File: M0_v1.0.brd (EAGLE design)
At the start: 68.6 x 53.3 mm, 61 parts, among them CN1 POWER_JACK, CN2 47346-0001, CN3 DIGITAL10, CN4 DIGITAL8, CN5 ICSP, CN6 POWER8, CN7 ANALOG6, CN8 SWD, CN9 UART, IC1 AMS1117-5.0, IC2 AMS1117-3.3, IC3 74LVC1G125DCK, Q2 32.768KHz, T1 AO3401A, T2 2N7002, U1 ATSAMD21G-AU, U2 ATSAMD21G-MU

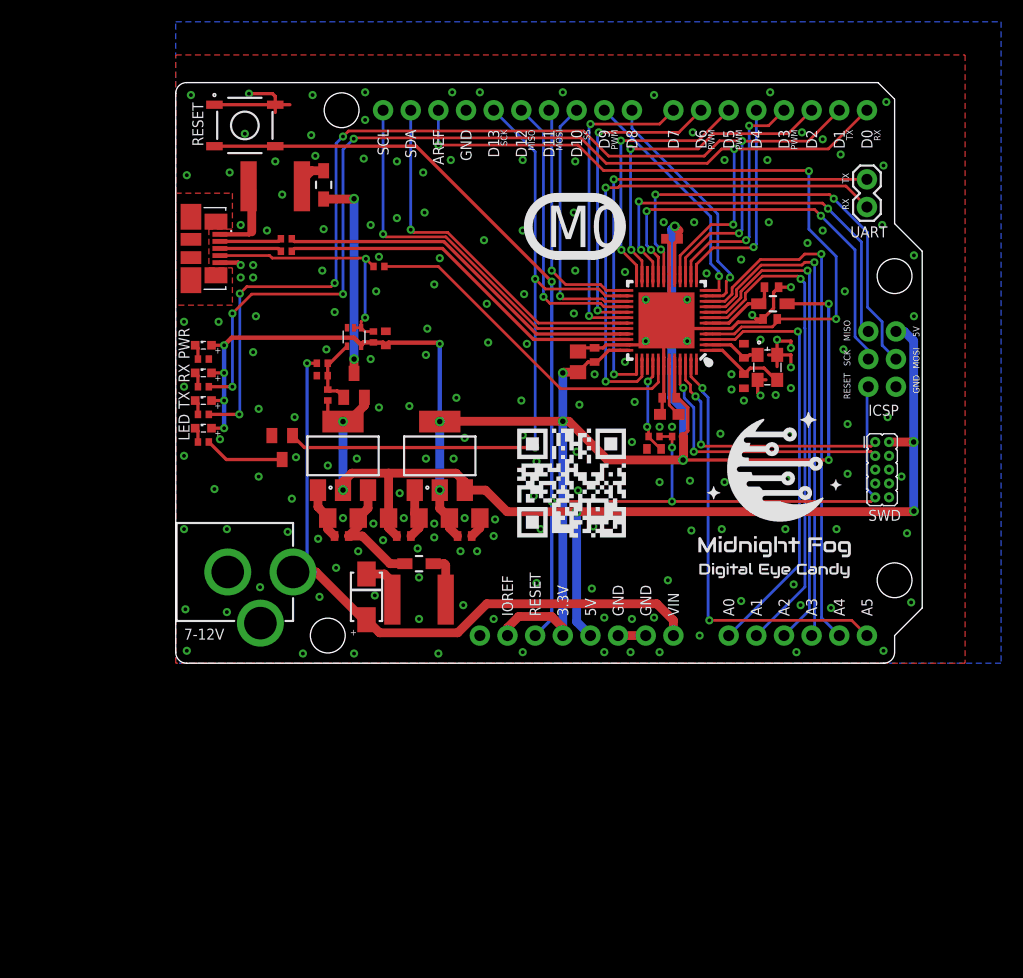
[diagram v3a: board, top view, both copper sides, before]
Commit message: Change the quote. Add some vias. move some traces around.
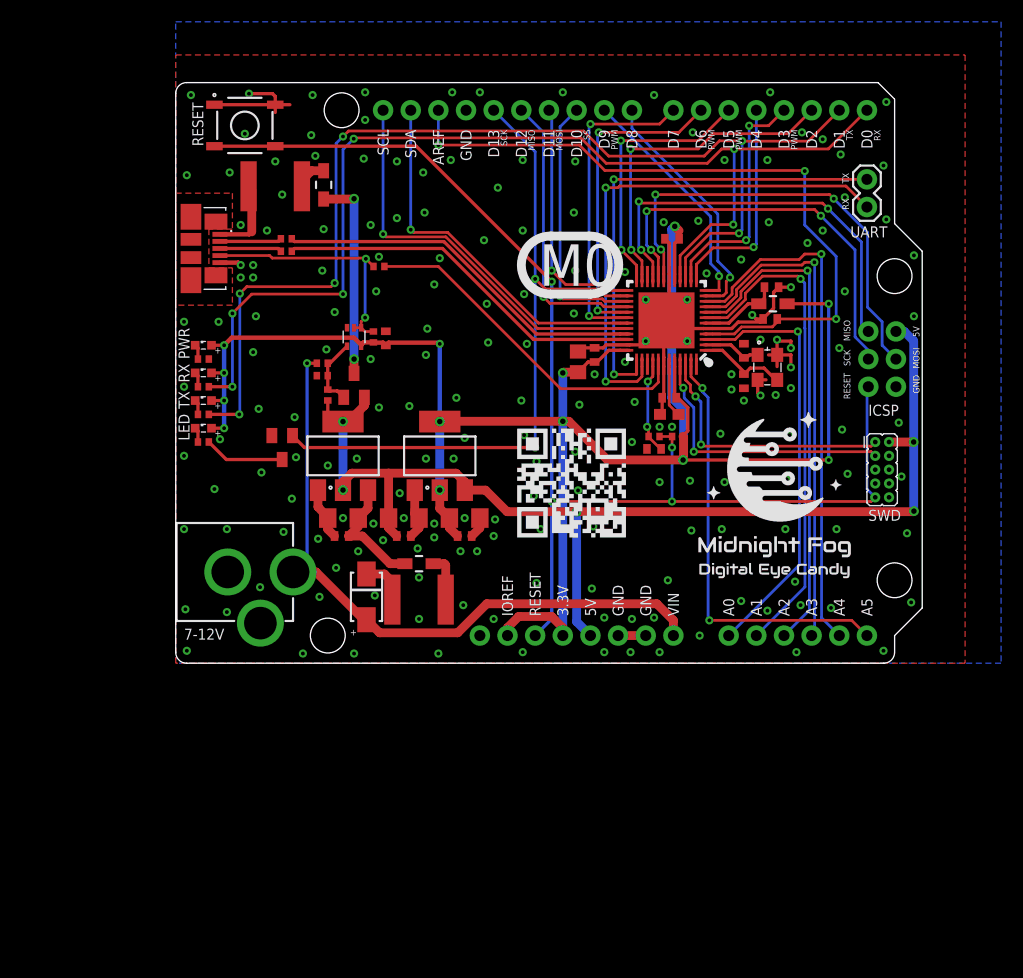
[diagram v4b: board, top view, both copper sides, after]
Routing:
- net GND: vias 191 -> 194
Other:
- board text added: "It always seems impossible until it is done. -- Nelson Mandela"
- board text removed: "Logic will get you from A to B. Imagination will take you everywhere. -- Albert Einstein"
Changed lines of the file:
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@@
 <text x="33.528" y="4.318" size="1.016" layer="21" font="vector" ratio="12" rot="R90">RESET</text>
 <text x="30.988" y="4.318" size="1.016" layer="21" font="vector" ratio="12" rot="R90">IOREF</text>
-<text x="34.036" y="38.227" size="3.81" layer="21" font="vector" ratio="16">M0</text>
-<wire x1="35.052" y1="37.465" x2="38.354" y2="37.465" width="0.8128" layer="21"/>
-<wire x1="35.052" y1="37.465" x2="35.052" y2="42.799" width="0.8128" layer="21" curve="-180"/>
-<wire x1="35.052" y1="42.799" x2="38.227" y2="42.799" width="0.8128" layer="21"/>
-<wire x1="38.227" y1="42.799" x2="38.354" y2="37.465" width="0.8128" layer="21" curve="-180"/>
+<text x="33.401" y="34.671" size="3.81" layer="21" font="vector" ratio="16">M0</text>
+<wire x1="34.417" y1="33.909" x2="38.1" y2="33.909" width="0.8128" layer="21"/>
+<wire x1="34.417" y1="33.909" x2="34.417" y2="39.243" width="0.8128" layer="21" curve="-180"/>
+<wire x1="34.417" y1="39.243" x2="37.973" y2="39.243" width="0.8128" layer="21"/>
+<wire x1="37.973" y1="39.243" x2="38.1" y2="33.909" width="0.8128" layer="21" curve="-180"/>
 <text x="0.762" y="2.159" size="1.016" layer="21" font="vector" ratio="12">7-12V</text>
 <text x="25.4" y="38.1" size="1.27" layer="22" font="vector" ratio="16" rot="MR0">M0 v1.0
@@
 <circle x="23.114" y="16.129" radius="0.127" width="0.1524" layer="21"/>
 <circle x="3.556" y="52.197" radius="0.127" width="0.1524" layer="21"/>
-<text x="25.4" y="21.59" size="1.27" layer="22" font="vector" ratio="16" rot="MR0">Logic will get you
-from A to B.
-Imagination will
-take you everywhere.
-    -- Albert Einstein</text>
+<text x="25.4" y="22.86" size="1.27" layer="22" font="vector" ratio="16" rot="MR0">It always seems impossible
+until it is done.
+    -- Nelson Mandela</text>
 <text x="61.849" y="44.069" size="0.6096" layer="21" font="vector" ratio="12" rot="R90">TX</text>
 <text x="61.849" y="41.656" size="0.6096" layer="21" font="vector" ratio="12" rot="R90">RX</text>
@@
 <via x="65.278" y="51.562" extent="1-16" drill="0.35"/>
 <via x="67.818" y="37.465" extent="1-16" drill="0.35"/>
-<via x="64.897" y="40.259" extent="1-16" drill="0.35"/>
+<via x="65.278" y="40.767" extent="1-16" drill="0.35"/>
 <via x="67.818" y="31.877" extent="1-16" drill="0.35"/>
 <via x="0.762" y="12.319" extent="1-16" drill="0.35"/>
@@
 <wire x1="22.355" y1="12.434" x2="21.605" y2="11.684" width="0.8128" layer="1"/>
 <via x="33.147" y="18.542" extent="1-16" drill="0.35"/>
-<via x="31.877" y="20.955" extent="1-16" drill="0.35"/>
+<via x="32.004" y="20.955" extent="1-16" drill="0.35"/>
 <contactref element="U1" pad="18"/>
 <contactref element="U1" pad="35"/>
@@
 <via x="48.768" y="35.814" extent="1-16" drill="0.35"/>
 <via x="51.943" y="37.084" extent="1-16" drill="0.35"/>
-<via x="47.625" y="40.513" extent="1-16" drill="0.35"/>
+<via x="48.006" y="40.64" extent="1-16" drill="0.35"/>
 <via x="59.436" y="39.751" extent="1-16" drill="0.35"/>
 <via x="54.483" y="40.513" extent="1-16" drill="0.35"/>
@@
 <via x="7.62" y="23.368" extent="1-16" drill="0.35"/>
 <via x="11.049" y="18.923" extent="1-16" drill="0.35"/>
-<via x="10.287" y="12.065" extent="1-16" drill="0.35"/>
+<via x="9.906" y="12.065" extent="1-16" drill="0.35"/>
 <via x="10.668" y="15.113" extent="1-16" drill="0.35"/>
-<via x="7.62" y="17.145" extent="1-16" drill="0.35"/>
+<via x="7.874" y="17.526" extent="1-16" drill="0.35"/>
 <via x="48.895" y="27.686" extent="1-16" drill="0.35"/>
 <via x="50.038" y="21.082" extent="1-16" drill="0.35"/>
@@
 <via x="67.183" y="11.938" extent="1-16" drill="0.35"/>
 <via x="66.675" y="17.145" extent="1-16" drill="0.35"/>
-<via x="65.405" y="22.606" extent="1-16" drill="0.35"/>
-<via x="61.722" y="21.971" extent="1-16" drill="0.35"/>
+<via x="66.421" y="22.098" extent="1-16" drill="0.35"/>
+<via x="61.214" y="21.463" extent="1-16" drill="0.35"/>
 <via x="61.468" y="34.163" extent="1-16" drill="0.35"/>
-<via x="61.341" y="28.829" extent="1-16" drill="0.35"/>
+<via x="60.96" y="28.956" extent="1-16" drill="0.35"/>
 <via x="60.198" y="5.08" extent="1-16" drill="0.35"/>
-<via x="56.769" y="7.239" extent="1-16" drill="0.35"/>
+<via x="56.896" y="7.493" extent="1-16" drill="0.35"/>
 <via x="57.404" y="5.334" extent="1-16" drill="0.35"/>
 <via x="56.007" y="12.319" extent="1-16" drill="0.35"/>
@@
 <via x="37.084" y="23.749" extent="1-16" drill="0.35"/>
 <via x="44.45" y="16.637" extent="1-16" drill="0.35"/>
-<via x="36.83" y="19.431" extent="1-16" drill="0.35"/>
+<via x="36.703" y="19.431" extent="1-16" drill="0.35"/>
 <via x="36.957" y="15.875" extent="1-16" drill="0.35"/>
 <via x="47.498" y="48.768" extent="1-16" drill="0.35"/>
@@
 <wire x1="48.485" y1="30.746" x2="47.31695" y2="30.746" width="0.3048" layer="1"/>
 <wire x1="47.31695" y1="30.746" x2="47.2028" y2="30.86015" width="0.3048" layer="1"/>
+<via x="54.356" y="4.826" extent="1-16" drill="0.35"/>
+<via x="29.591" y="43.688" extent="1-16" drill="0.35"/>
+<via x="61.468" y="42.799" extent="1-16" drill="0.35"/>
 </signal>
 <signal name="VIN" class="3">
@@
 <via x="60.6722" y="31.623" extent="1-16" drill="0.35"/>
 <wire x1="60.6722" y1="31.623" x2="60.6722" y2="37.3718" width="0.254" layer="16"/>
-<wire x1="60.6722" y1="37.3718" x2="58.166" y2="39.878" width="0.254" layer="16"/>
-<wire x1="58.166" y1="39.878" x2="58.166" y2="45.212" width="0.254" layer="16"/>
-<via x="58.166" y="45.212" extent="1-16" drill="0.35"/>
+<wire x1="60.6722" y1="37.3718" x2="57.785" y2="40.259" width="0.254" layer="16"/>
+<wire x1="57.785" y1="40.259" x2="57.785" y2="45.212" width="0.254" layer="16"/>
+<via x="57.785" y="45.212" extent="1-16" drill="0.35"/>
 <via x="24.13" y="47.6024" extent="1-16" drill="0.35"/>
-<wire x1="58.166" y1="45.212" x2="58.1124" y2="45.2656" width="0.254" layer="1"/>
-<wire x1="58.1124" y1="45.2656" x2="39.2938" y2="45.2656" width="0.254" layer="1"/>
-<wire x1="39.2938" y1="45.2656" x2="36.957" y2="47.6024" width="0.254" layer="1"/>
-<wire x1="36.957" y1="47.6024" x2="24.13" y2="47.6024" width="0.254" layer="1"/>
+<wire x1="57.785" y1="45.212" x2="57.7314" y2="45.2656" width="0.254" layer="1"/>
+<wire x1="57.7314" y1="45.2656" x2="39.4208" y2="45.2656" width="0.254" layer="1"/>
+<wire x1="39.4208" y1="45.2656" x2="37.084" y2="47.6024" width="0.254" layer="1"/>
+<wire x1="37.084" y1="47.6024" x2="24.13" y2="47.6024" width="0.254" layer="1"/>
 <wire x1="24.13" y1="47.6024" x2="24.13" y2="50.8" width="0.254" layer="16"/>
 </signal>

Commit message: Moved main MCU to the right with all belongings. Corrected JTAG orientation and position. Add proper pin descriptions. Moved some wires for easier routing.
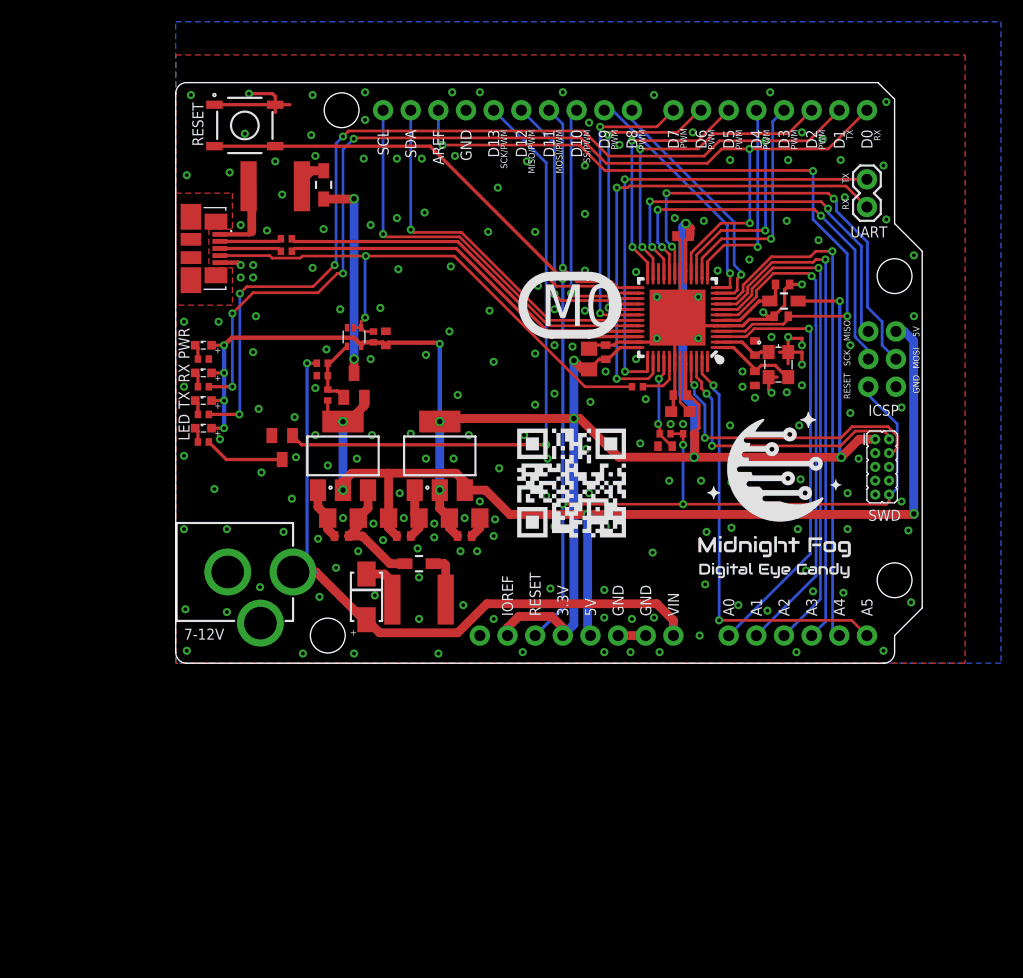
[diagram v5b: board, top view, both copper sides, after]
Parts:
- moved R6 26.2 mm to (42.4, 25.4)
- moved L3 1.05 mm to (55.9, 33.3)
- moved C15 1.05 mm to (46.6, 39.2)
- moved C9 1.05 mm to (55.8, 34.8)
- moved C16 1.05 mm to (46.4, 24.6)
- moved C17 1.05 mm to (38.0, 27.9)
- moved C7 1.05 mm to (46.4, 23.1)
- moved C8 1.05 mm to (45.0, 19.9)
- moved R12 1.05 mm to (47.1, 21.1)
- moved R3 1.05 mm to (45.0, 21.1)
- moved U1 1.05 mm to (46.1, 31.8)
- moved U2 1.05 mm to (46.1, 31.8)
- moved C12 1.05 mm to (53.2, 26.2)
- moved C13 1.05 mm to (53.2, 29.0)
- moved C14 1.05 mm to (39.5, 28.6)
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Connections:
- net 3.3V: now also CN8.1
- net 5V: no longer CN8.2
- net GND: now also CN8.3, CN8.5, CN8.9; no longer CN8.10, CN8.4, CN8.6
- net RESET: now also CN8.10; no longer CN8.9
- net SWDCLK: now also CN8.4; no longer CN8.3
- net SWDIO: now also CN8.2; no longer CN8.1
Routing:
- net XUSB_EN: track 23.0 -> 51.7 mm
- net USB_EN: track 32.4 -> 5.00 mm
- net 3.3V: track 183.2 -> 190.2 mm
- net RESET: track 116.8 -> 120.6 mm
- net SWDCLK: track 26.0 -> 28.7 mm
- net 5V: track 105.9 -> 103.3 mm, vias 5 -> 4
- net SWDIO: track 24.8 -> 26.3 mm
- net D7: track 29.6 -> 28.3 mm
- net D6_PWM: track 29.6 -> 28.3 mm
- net UART_TX: track 44.8 -> 43.5 mm
- net UART_RX: track 48.0 -> 46.7 mm
- net SPI_MISO: track 38.5 -> 37.3 mm
- net D5_PWM: track 24.8 -> 23.5 mm
- net SPI_SCK: track 38.4 -> 37.2 mm
- net SPI_MOSI: track 42.1 -> 41.0 mm
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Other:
- board text added: "MISO/PWM"
- board text added: "MOSI/PWM"
- board text added: "SCK/PWM"
- board text added: "SS/PWM"
- board text removed: "SS"

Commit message: Moved few stuff around.
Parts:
- moved R11 1.82 mm to (16.4, 29.6)
- moved IC3 1.82 mm to (14.6, 29.6)
- moved C11 1.80 mm to (17.5, 29.6)
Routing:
- net XUSB_EN: track 51.7 -> 53.6 mm
- net N$12: track 6.60 -> 5.37 mm
- net SCL: track 38.5 -> 37.6 mm

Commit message: Move some stuff around
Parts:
- moved Q2 1.65 mm to (55.4, 25.8)
- moved C13 1.53 mm to (54.6, 28.3), turned to 180 degrees
- moved C19 0.99 mm to (56.4, 31.2)
- moved C12 0.76 mm to (53.2, 25.4)
- moved C9 0.72 mm to (56.3, 34.3)
- moved L3 0.64 mm to (56.3, 32.8)
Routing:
- net GND: track 69.1 -> 70.6 mm, vias 203 -> 208
- net A0: track 40.4 -> 39.3 mm
- net A1: track 46.4 -> 45.4 mm
- net MCU_OSC32_OUT: track 5.58 -> 6.55 mm
- net A3: track 47.4 -> 46.5 mm
- net A2: track 46.8 -> 45.9 mm
- net 3.3V: track 189.9 -> 189.0 mm
- net A4: track 48.5 -> 47.7 mm
- net AREF: track 65.9 -> 66.8 mm
- net MCU_OSC32_IN: track 8.48 -> 9.02 mm

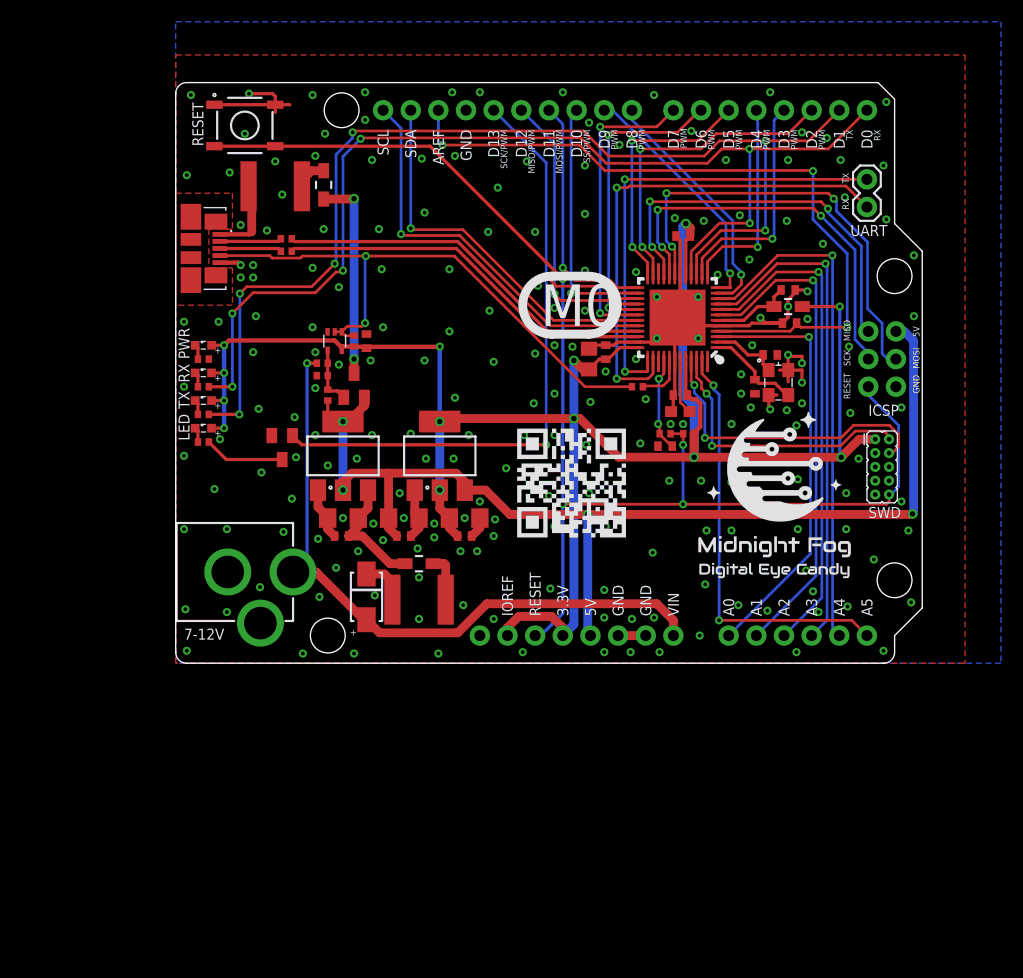
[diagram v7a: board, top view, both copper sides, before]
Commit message: Move some traces around. Reduced number of isolated areas of copper.
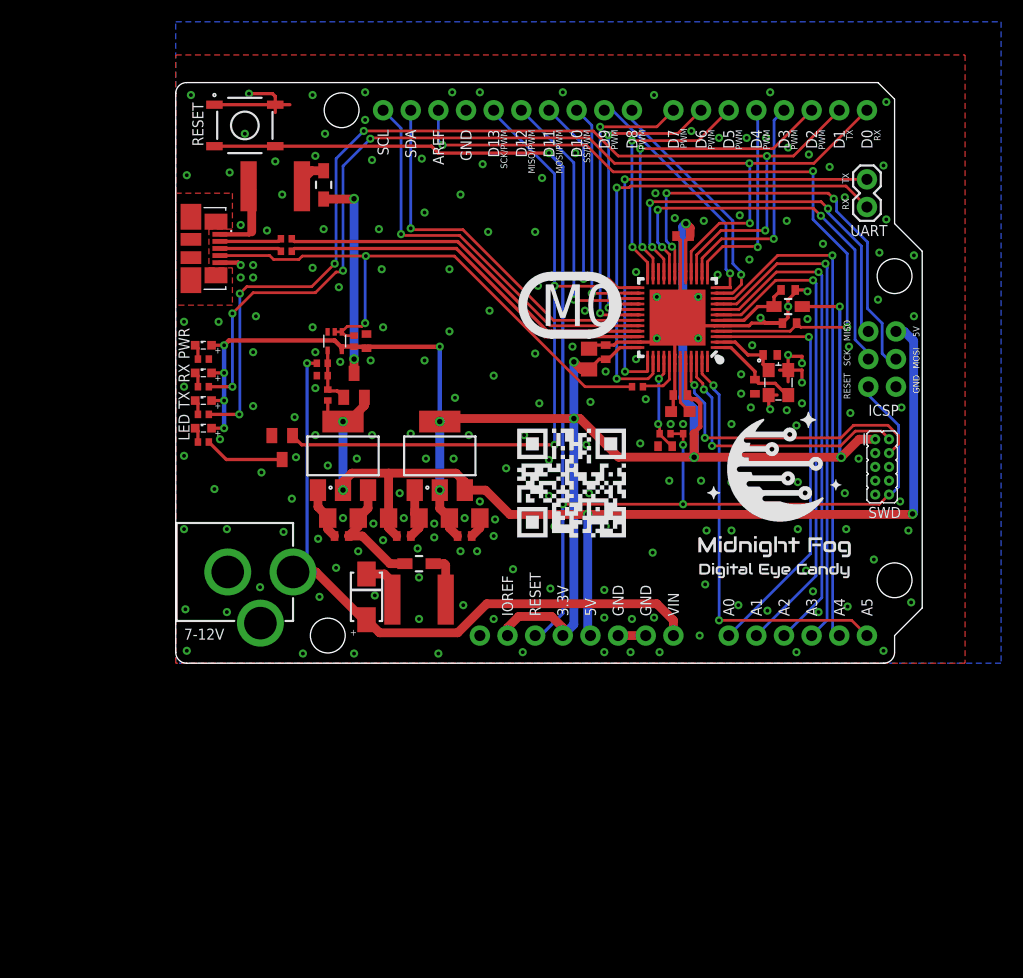
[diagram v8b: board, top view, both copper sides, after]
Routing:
- net RESET: track 121.0 -> 126.7 mm
- net D1_TX: track 101.8 -> 100.0 mm
- net D0_RX: track 99.0 -> 97.1 mm
- net D10_SS: track 23.6 -> 22.1 mm
- net D12_MISO: track 26.4 -> 25.7 mm
- net D11_MOSI: track 22.9 -> 22.4 mm
- net GND: vias 208 -> 206
